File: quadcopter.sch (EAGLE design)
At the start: 66 parts, among them J1 ISP, J3 POWER_JACKPTH_LOCK, M1 MOTOR_PADS, M2 MOTOR_PADS, M3 MOTOR_PADS, M4 MOTOR_PADS, U1 ATMEGA128RFA1, U2 LM1117, Y1 16MHz, Y2 32.768kHz

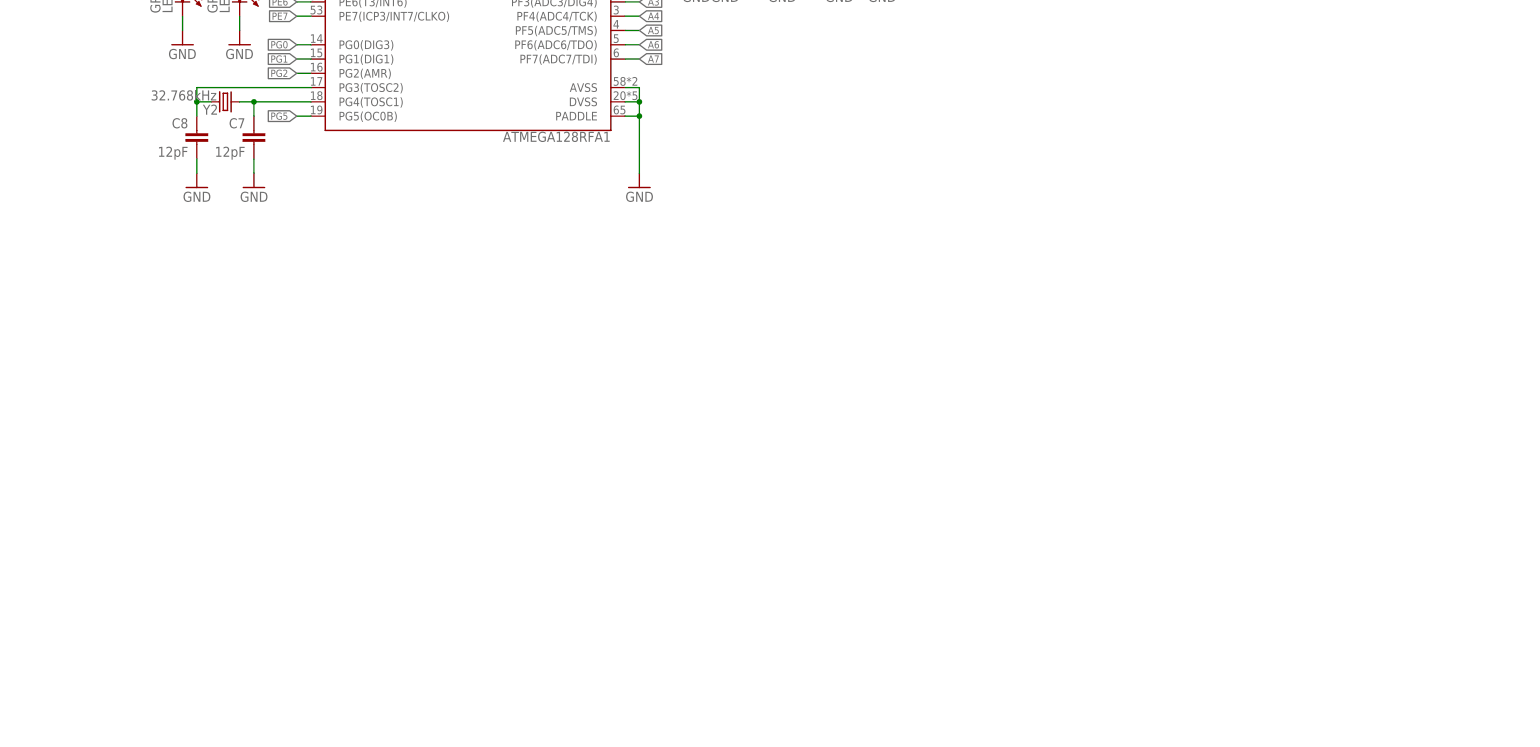
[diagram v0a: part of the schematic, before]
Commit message: voltage reg added
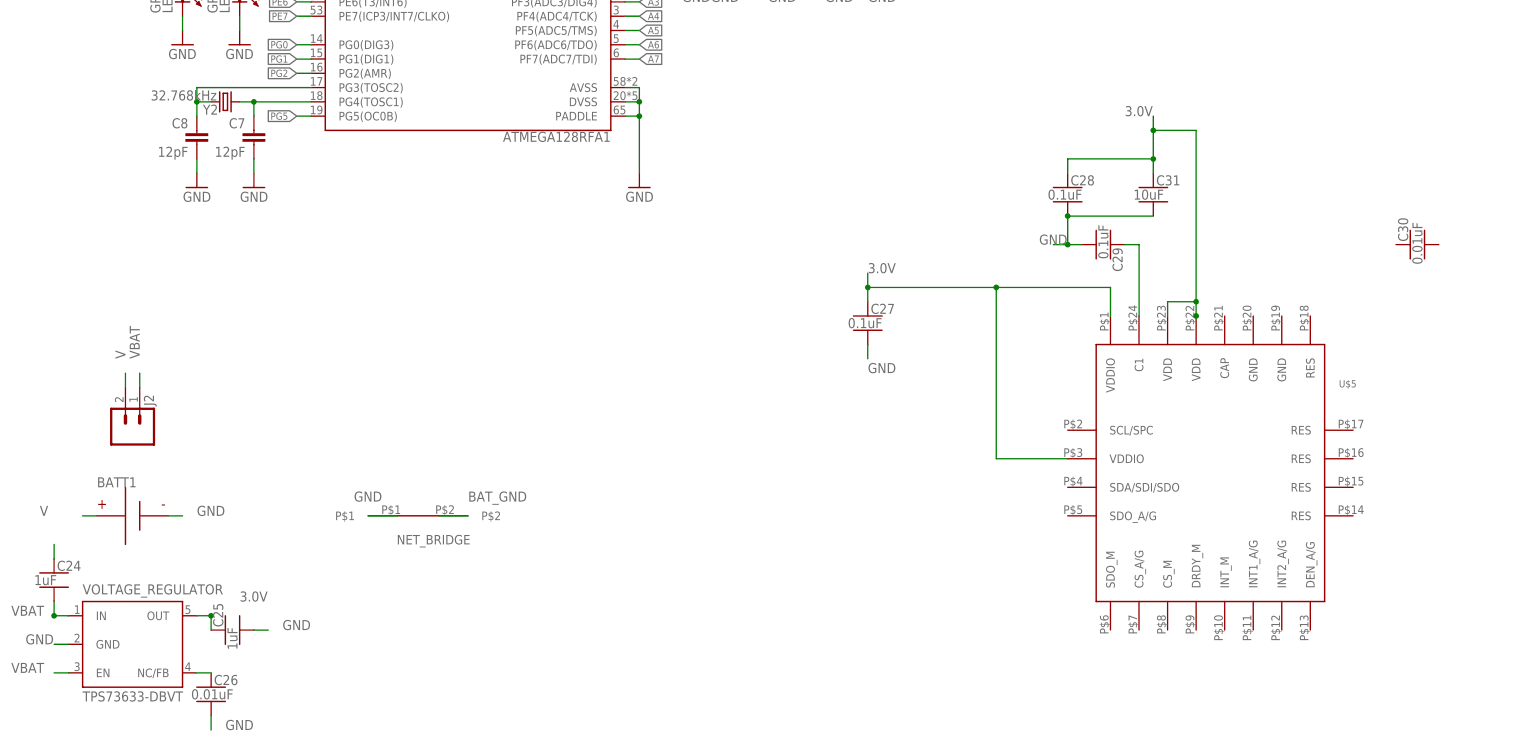
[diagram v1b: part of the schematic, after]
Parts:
- added BATT1: BATTERY-HUBSAN-W/HOLDER, quadparts_prebuilt:BATTERY-HUBSAN-W/HOLDER
- added C24, C25: 1uF, quadparts_prebuilt:CAPACITOR-NP_SMD-2012-0805_CERAMIC-1UF
- added C26, C30: 0.01uF, quadparts_prebuilt:CAPACITOR-NP_SMD-2012-0805_CERAMIC-0.01UF
- added C27, C28, C29: 0.1uF, quadparts_prebuilt:CAPACITOR-NP_SMD-2012-0805_CERAMIC-0.1UF
- added C31: 10uF, quadparts_prebuilt:CAPACITOR-NP_SMD-2012-0805_CERAMIC-10UF
- added J2: (no value), quadparts_jay:MALE_HEADER_2POS-2X1-0.1IN
- added NET_BRIDGE: NET_BRIDGE, quadparts_jay:NET_BRIDGE
- added U$5: IMU_497-14946-1-ND, quadparts_jay:IMU_497-14946-1-ND
- added VOLTAGE_REGULATOR: TPS73633-DBVT, quadparts_prebuilt:TPS73633-DBVT
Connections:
- removed net 3V: C10.+, C12.1, C3.1, C4.1, R1.2, R2.2, R3.2, U1.DEVDD, U1.EVDD, U2.OUT
- new net 3.0V: C10.+, C12.1, C25.1, C27.1, C28.1, C3.1, C31.1, C4.1, R1.2, R2.2, R3.2, U$5.VDD@1, U$5.VDD@2, U$5.VDDIO@1, U$5.VDDIO@2, U1.DEVDD, U1.EVDD, U2.OUT, VOLTAGE_REGULATOR.OUT
- new net BAT_GND: C16.2, C17.-, C18.2, C19.-, C20.2, C21.-, C22.2, C23.-, NET_BRIDGE.P$2, R10.1, R12.1, R14.1, R8.1, U$1.S, U$2.S, U$3.S, U$4.S
- new net N$1: C24.1
- new net N$10: C29.1, U$5.C1
- new net N$18: C26.1, VOLTAGE_REGULATOR.NC/FB
- new net V: BATT1.P, J2.2
- new net VBAT: C17.+, C19.+, C21.+, C23.+, C24.2, D1.C, D2.C, D3.C, D4.C, J2.1, M1.V+, M2.V+, M3.V+, M4.V+, VOLTAGE_REGULATOR.EN, VOLTAGE_REGULATOR.IN
- net GND: now also BATT1.N, C25.2, C26.2, C27.2, C28.2, C29.2, C31.2, NET_BRIDGE.P$1, VOLTAGE_REGULATOR.GND; no longer C16.2, C17.-, C18.2, C19.-, C20.2, C21.-, C22.2, C23.-, R10.1, R12.1, R14.1, R8.1, U$1.S, U$2.S, U$3.S, U$4.S
- net VCC: no longer C17.+, C19.+, C21.+, C23.+, D1.C, D2.C, D3.C, D4.C, M1.V+, M2.V+, M3.V+, M4.V+

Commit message: Finish MC, Breakout, and Motors
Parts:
- removed B1: 748421245, SparkFun-RF:BALUN0805
- removed C10, C14: 10uF, SparkFun-Passives:CAP_POL1206
- removed C11: 22pF, SparkFun-Passives:CAP0402-CAP
- removed C12: 1uF, SparkFun-Passives:CAP0402-CAP
- removed C13: 0.1uF, SparkFun-Passives:CAP0402-CAP
- removed C9: 0.75pF, SparkFun-Passives:CAP0402-CAP
- removed JP6: (no value), SparkFun-Connectors:M02JST-PTH-2
- removed JP7: (no value), SparkFun-Connectors:M021X02_NO_SILK
- removed JP8: (no value), SparkFun-Connectors:M023.5MM-NO_SILK
- removed LED1: RED, SparkFun-LED:LED0603
- removed LED2, LED3: GREEN, SparkFun-LED:LED0603
- removed R2: 1k, SparkFun-Passives:RESISTOR0402-RES
- removed R3: 240, SparkFun:RESISTOR0402-RES
- removed R4: 390, SparkFun:RESISTOR0402-RES
- removed S2: (no value), SparkFun:SWITCH-SPST-SMD-A
- removed U2: LM1117, SparkFun:V_REG_317SMD
- removed Y2: 32.768kHz, SparkFun-FreqCtrl:CRYSTAL32-SMD
- added B2: BALUN0805, quadparts_prebuilt:BALUN0805
- added D5, D6: green, quadparts_prebuilt:DIODE-LED_SMD-2012-0805-GREEN
- C1, C2: device SparkFun-Passives:CAP0402-CAP -> quadparts_prebuilt:CAPACITOR-NP_SMD-2012-0805_CERAMIC-1UF
- C3, C4: value 1uF -> 12pF; device SparkFun-Passives:CAP0402-CAP -> quadparts_prebuilt:CAPACITOR-NP_SMD-2012-0805_CERAMIC-12PF
- C5: value 12pF -> 0.75pF; device SparkFun-Passives:CAP0402-CAP -> quadparts_prebuilt:CAPACITOR-NP_SMD-2012-0805_CERAMIC-0.75PF
- C6: value 12pF -> 22pF; device SparkFun-Passives:CAP0402-CAP -> quadparts_prebuilt:CAPACITOR-NP_SMD-2012-0805_CERAMIC-22PF
- C7, C8: value 12pF -> 1uF; device SparkFun-Passives:CAP0402-CAP -> quadparts_prebuilt:CAPACITOR-NP_SMD-2012-0805_CERAMIC-1UF
- J3: value POWER_JACKPTH_LOCK -> (none); device SparkFun-Connectors:POWER_JACKPTH_LOCK -> quadparts_prebuilt:SIP-10_TH-254X10-1
- R1: value 10k -> 10K; device SparkFun-Passives:RESISTOR0402-RES -> quadparts_prebuilt:RESISTOR_SMD-2012-0805-10K
- R5, R6: device SparkFun:RESISTOR0402-RES -> quadparts_prebuilt:RESISTOR_SMD-2012-0805-330
- Y1: value 16MHz -> (none); device SparkFun-FreqCtrl:CRYSTAL5X3 -> quadparts_prebuilt:CRYSTAL5X3
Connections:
- removed net FB: R3.1, R4.2, U2.ADJ
- removed net FILTERED: R10.2, R11.2, R12.2, R13.2, R14.2, R7.2, R8.2, R9.2
- removed net FLYBACK: D1.A, D2.A, D3.A, D4.A, M1.V-, M2.V-, M3.V-, M4.V-, U$1.D, U$2.D, U$3.D, U$4.D
- removed net N$2: LED1.A, R2.1
- removed net N$5: C7.1, U1.PG4(TOSC1), Y2.1
- removed net N$6: C8.1, U1.PG3(TOSC2), Y2.2
- removed net N$9: J3.PWR, JP6.2, JP7.2, JP8.2, S2.P
- removed net VCC: C13.1, C14.+, S2.O, U2.IN
- new net FILTERED1: R13.2, R14.2
- new net FILTERED2: R10.2, R9.2
- new net FILTERED3: R11.2, R12.2
- new net FILTERED4: R7.2, R8.2
- new net FLYBACK1: D4.A, M4.V-, U$4.D
- new net FLYBACK2: D2.A, M2.V-, U$2.D
- new net FLYBACK3: D3.A, M3.V-, U$3.D
- new net FLYBACK4: D1.A, M1.V-, U$1.D
- net 3.0V: now also C7.1, C8.1, J3.7; no longer C10.+, C12.1, C3.1, C4.1, R2.2, R3.2, U2.OUT
- net AVDD: now also C2.1; no longer C1.1
- net BAT_GND: now also J3.9
- net DVDD: now also C1.1; no longer C2.1
- net GND: now also B2.IN, C6.1, D5.C, D6.C, J3.10; no longer B1.GND@5, C10.-, C11.2, C12.2, C13.2, C14.-, C6.2, C9.1, J3.GND, J3.GNDBREAK, JP6.1, JP7.1, JP8.1, LED1.C, LED2.C, LED3.C, R4.1
- net N$13: now also D6.A; no longer LED2.A
- net N$3: now also C4.1; no longer C5.1
- net N$4: now also C3.1; no longer C6.1
- net N$7: now also B2.GND@2, C6.2; no longer B1.GND@2, C11.1
- net N$8: now also D5.A; no longer LED3.A
- net PB5: now also J3.6
- net PE3: now also J3.4
- net PE4: now also J3.3
- net PE5: now also J3.5
- net RFANT: now also B2.GND@5, C5.1; no longer B1.IN, C9.2
- net RFN: now also B2.OUT1; no longer B1.OUT2
- net RFP: now also B2.OUT2; no longer B1.OUT1
- net SCL: now also J3.1
- net SDA: now also J3.2
- net VBAT: now also J3.8
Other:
- note removed: "800mA"
- note removed: "ADJ - 3.3V"
- moved on the sheet: C22, C23, D4, J1, M4, R13, R14, U$4, Y1
